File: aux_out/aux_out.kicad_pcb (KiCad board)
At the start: 2 copper layers, 30 x 22.6 mm, 9 parts, among them J1 AudioJack2_SwitchT, J2 AudioJack2_SwitchT, J3 AudioJack3

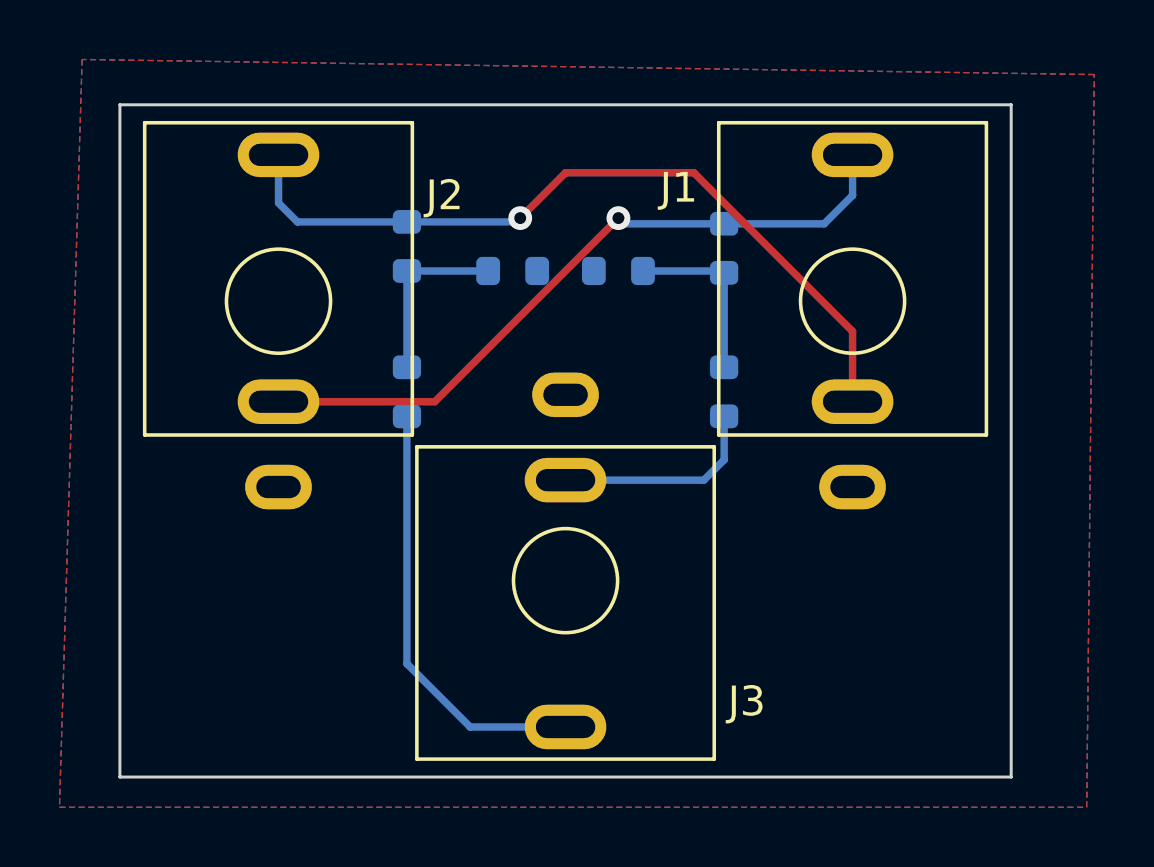
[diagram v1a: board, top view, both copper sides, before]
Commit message: Use relative paths for libraries
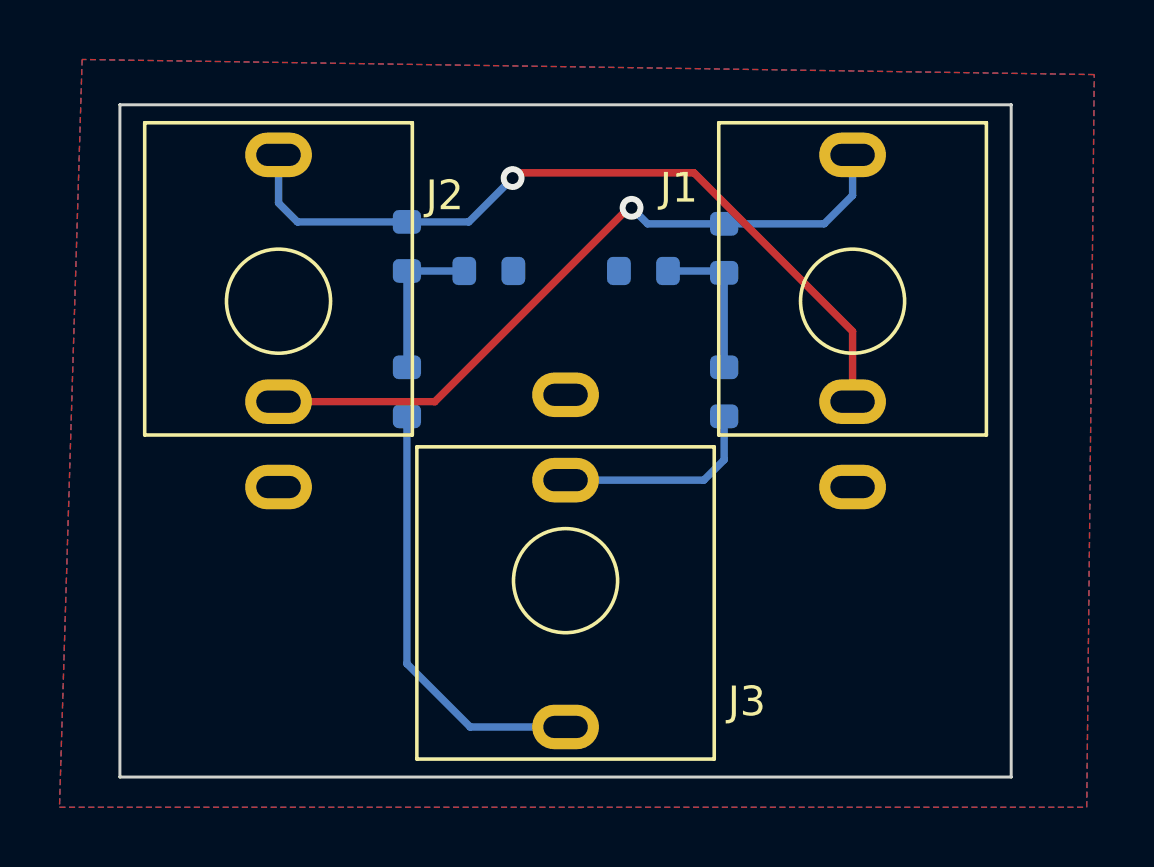
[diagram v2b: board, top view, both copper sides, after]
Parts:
- moved R1 0.84 mm to (147.4, 77.7)
- moved R5 0.80 mm to (142.2, 77.7)
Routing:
- net Net-(R1-Pad1): track 5.93 -> 5.09 mm
- net Net-(R4-Pad2): track 5.97 -> 5.17 mm

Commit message: Add AUX front panel
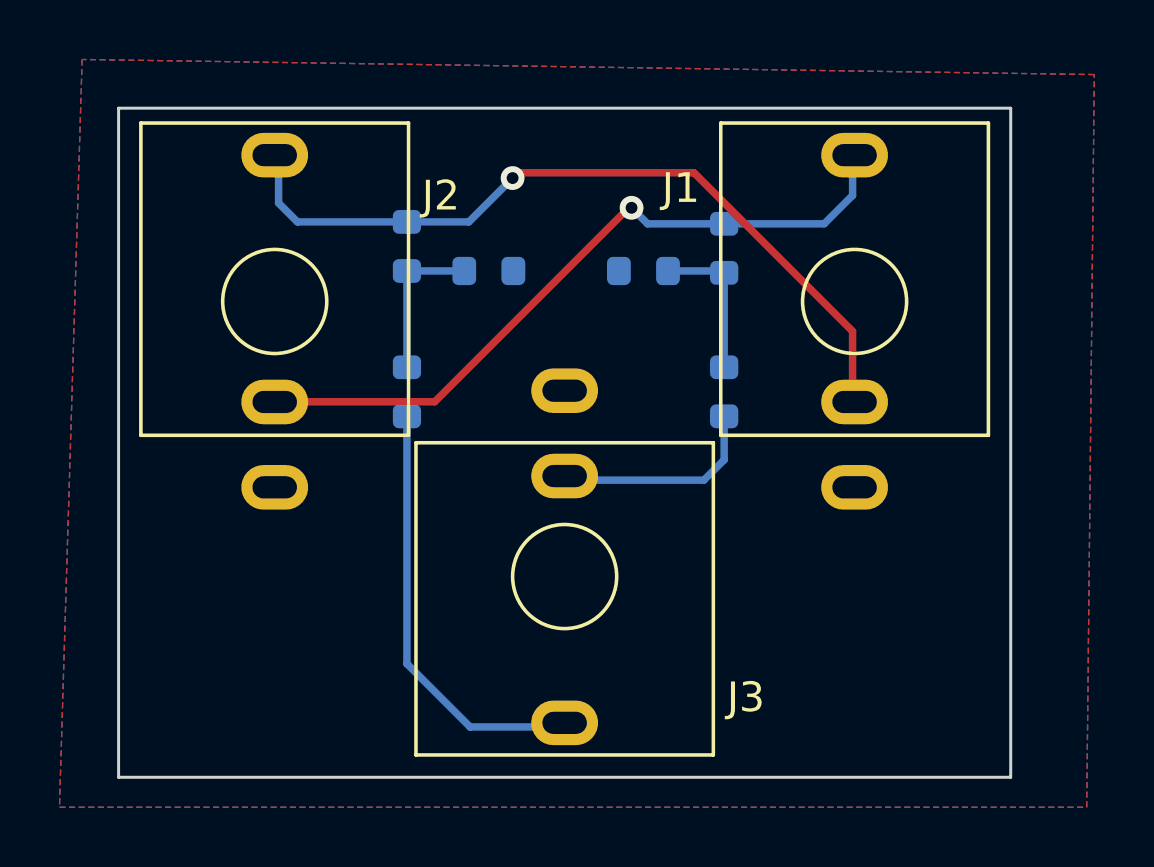
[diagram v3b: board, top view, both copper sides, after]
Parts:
- moved J3 0.14 mm to (144.8, 88.0)
- moved J2 0.13 mm to (135.0, 78.8)
- moved J1 0.07 mm to (154.5, 78.8)
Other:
- board size 30 x 22.6 mm -> 30 x 22.5 mm
- board text added: "Passive AUX out"
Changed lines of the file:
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@@
 	(net 7 "Net-(R4-Pad2)")
 	(footprint "custom_fp:PJ366ST"
+		(locked yes)
 		(layer "F.Cu")
-		(at 144.78 88.138 180)
+		(at 144.75 88 180)
 		(property "Reference" "J3"
 			(at -6.096 -4.064 0)
@@
 	)
 	(footprint "custom_fp:PJ398SM"
+		(locked yes)
 		(layer "F.Cu")
-		(at 135.128 78.74)
+		(at 135 78.75)
 		(property "Reference" "J2"
 			(at 5.588 -3.556 0)
@@
 	)
 	(footprint "custom_fp:PJ398SM"
+		(locked yes)
 		(layer "F.Cu")
-		(at 154.432 78.74)
+		(at 154.5 78.75)
 		(property "Reference" "J1"
 			(at -5.842 -3.81 0)
@@
 	)
 	(gr_line
-		(start 129.794 94.742)
-		(end 159.766 94.742)
+		(start 129.75 94.75)
+		(end 159.75 94.75)
 		(stroke
 			(width 0.1)
@@
 	)
 	(gr_line
-		(start 159.766 94.742)
-		(end 159.766 72.136)
+		(start 159.75 94.75)
+		(end 159.75 72.25)
 		(stroke
 			(width 0.1)
@@
 	)
 	(gr_line
-		(start 159.766 72.136)
-		(end 129.794 72.136)
+		(start 159.75 72.25)
+		(end 129.75 72.25)
 		(stroke
 			(width 0.1)
@@
 	)
 	(gr_line
-		(start 129.794 72.136)
-		(end 129.794 94.742)
+		(start 129.75 72.25)
+		(end 129.75 94.75)
 		(stroke
 			(width 0.1)
@@
 		(layer "Edge.Cuts")
 	)
+	(gr_text "Passive\nAUX out"
+		(at 135 90.4 0)
+		(layer "B.SilkS")
+		(effects
+			(font
+				(size 1 1)
+				(thickness 0.15)
+			)
+			(justify bottom mirror)
+		)
+	)
 	(segment
